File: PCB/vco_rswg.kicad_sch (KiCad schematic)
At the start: 19 parts, among them J6 VCO, Q1 2N5457, U1 LM324, U2 LM324

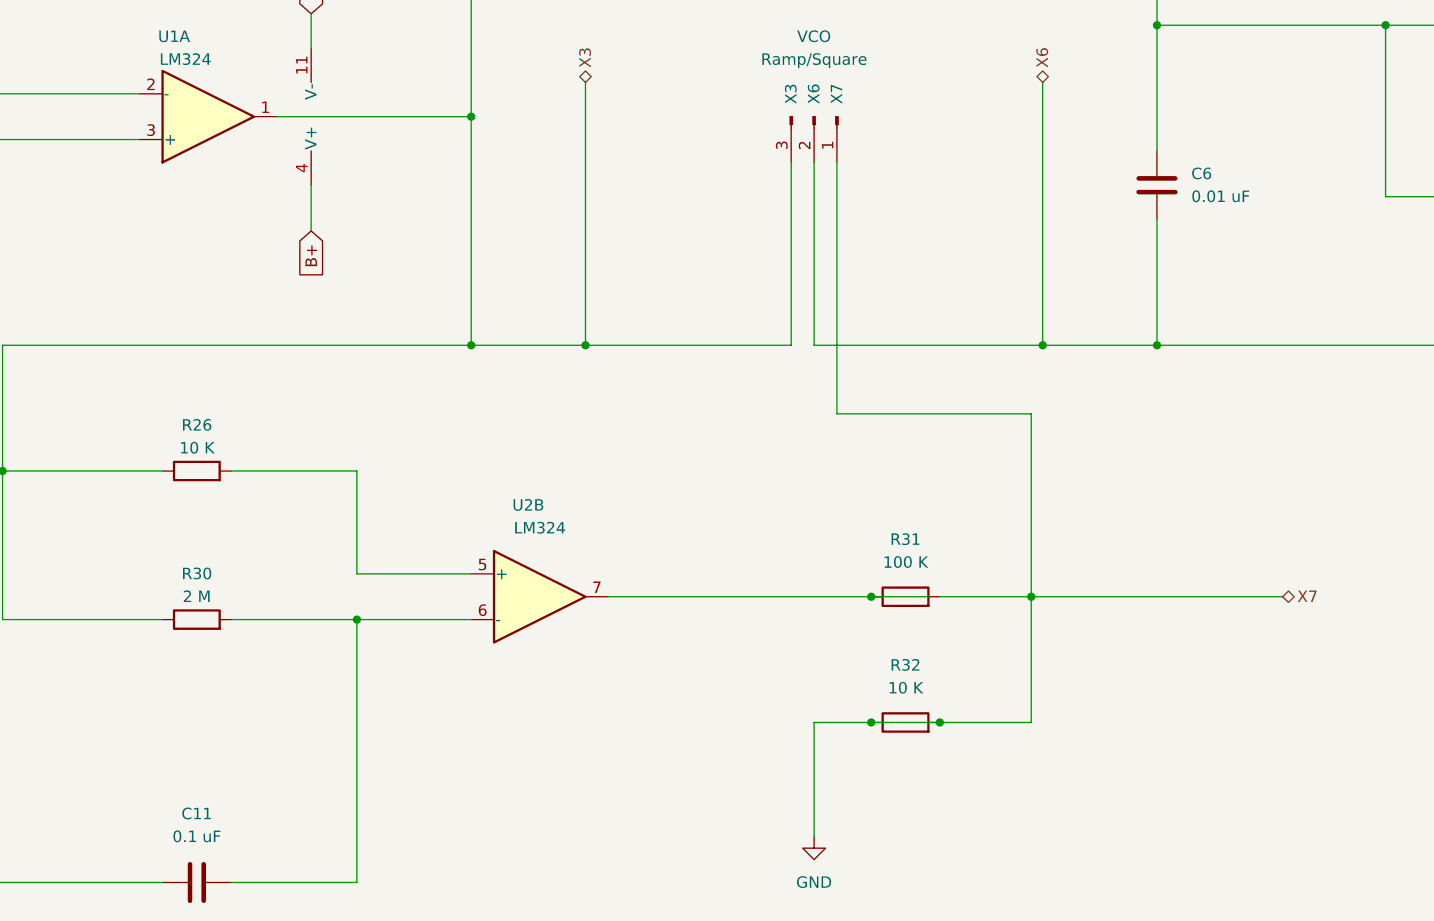
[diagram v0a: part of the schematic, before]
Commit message: Change TO-92 transistors to wide package to avoid shorting during soldering
Added B- hole for speaker
Added more vias to shorten traces
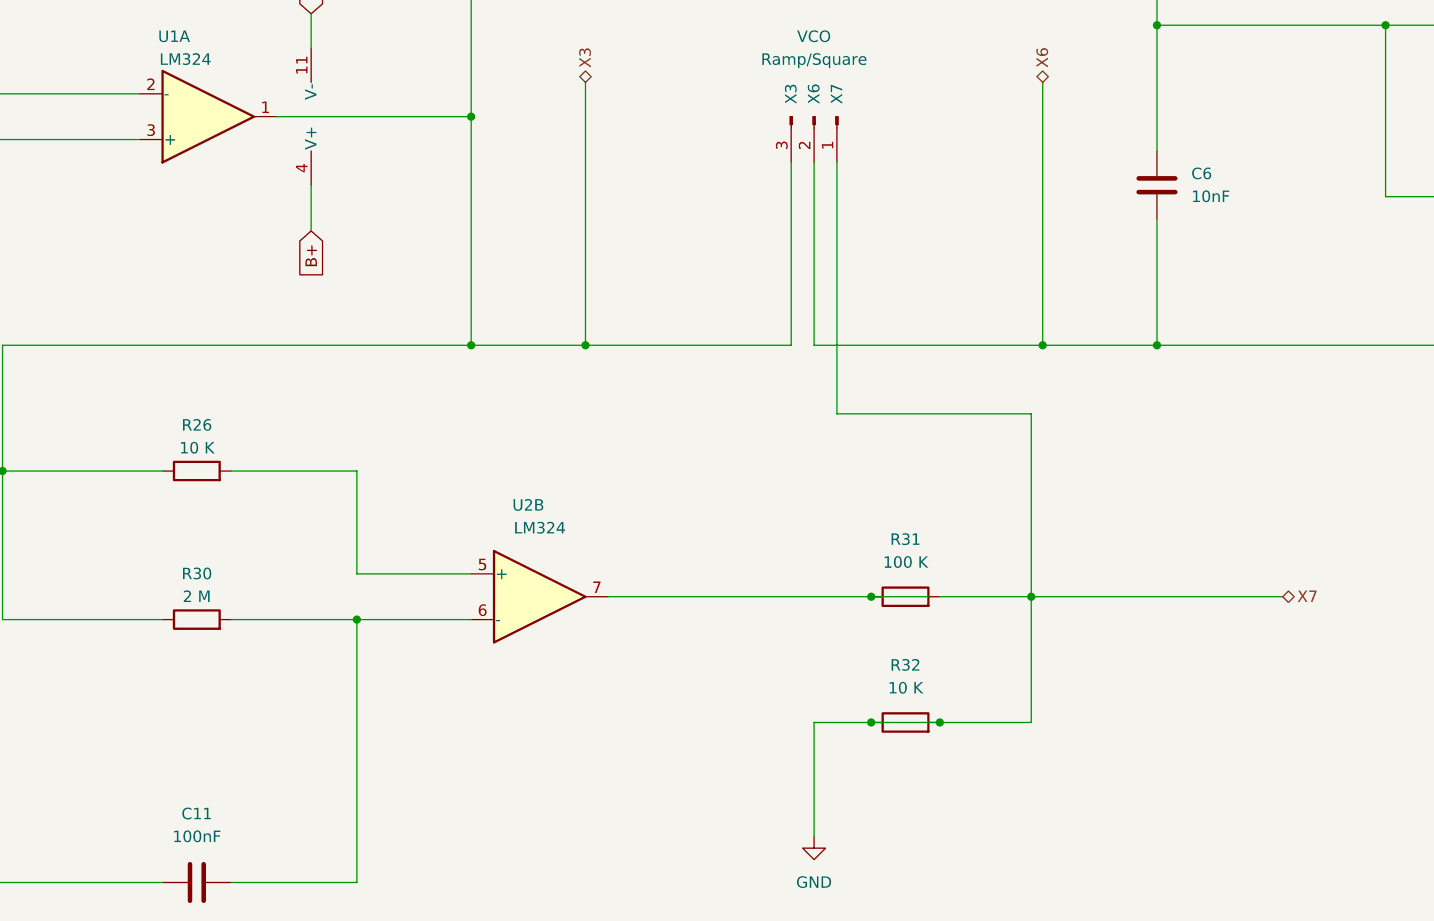
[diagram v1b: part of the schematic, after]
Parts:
- C11: value 0.1 uF -> 100nF
- C6: value 0.01 uF -> 10nF
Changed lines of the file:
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@@
 			)
 		)
-		(property "Value" "0.1 uF"
+		(property "Value" "100nF"
 			(at 58.42 172.72 90)
 			(show_name no)
@@
 		(fields_autoplaced yes)
 		(property "Reference" "C6"
-			(at 168.91 99.06 0)
+			(at 168.91 99.0599 0)
 			(show_name no)
 			(do_not_autoplace no)
@@
 			)
 		)
-		(property "Value" "0.01 uF"
-			(at 168.91 101.6 0)
+		(property "Value" "10nF"
+			(at 168.91 101.5999 0)
 			(show_name no)
 			(do_not_autoplace no)

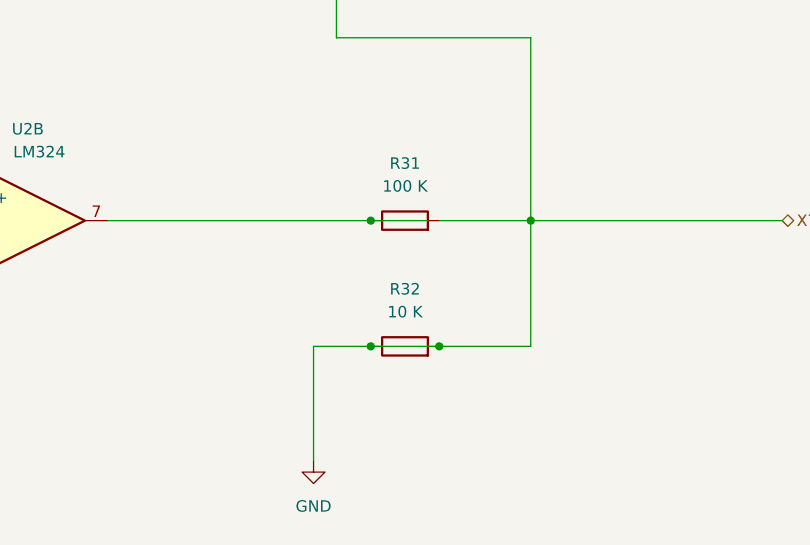
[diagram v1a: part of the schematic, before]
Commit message: Fix accidental short
Id reckon Tom tried to select these 3 traces and drag them, but the resistors didnt move along so he accidentally shorted R31, R32 and the square wave output of the VCO to the LPF
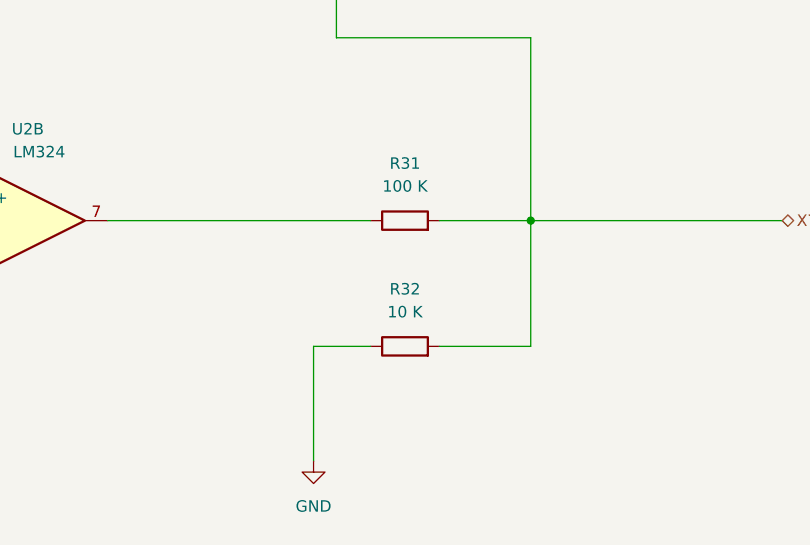
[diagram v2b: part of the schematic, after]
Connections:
- net GND: no longer J6.1 (Pin_1), R31.2, R32.2
- new net X7: J6.1 (Pin_1), R31.2, R32.2
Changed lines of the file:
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@@
-	)
-	(junction
-		(at 140.97 160.02)
-		(diameter 0)
-		(color 0 0 0 0)
 	)
 	(junction
@@
 	)
 	(junction
-		(at 133.35 146.05)
-		(diameter 0)
-		(color 0 0 0 0)
-	)
-	(junction
 		(at 88.9 118.11)
 		(diameter 0)
@@
 	)
 	(junction
-		(at 133.35 160.02)
-		(diameter 0)
-		(color 0 0 0 0)
-	)
-	(junction
 		(at 36.83 132.08)
 		(diameter 0)
@@
 	(wire
 		(pts
-			(xy 139.7 146.05) (xy 133.35 146.05)
-		)
-		(stroke
-			(width 0)
-			(type default)
-		)
-	)
-	(wire
-		(pts
 			(xy 212.09 101.6) (xy 190.5 101.6)
 		)
@@
 		)
 		(stroke
-			(width 0)
-			(type default)
-		)
-	)
-	(wire
-		(pts
-			(xy 133.35 160.02) (xy 140.97 160.02)
-		)
-		(stroke

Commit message: Necessary Changes to Schematic and PCB
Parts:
- J6: footprint Connector_PinHeader_2.00mm:PinHeader_1x03_P2.00mm_Vertical -> Connector_PinSocket_2.54mm:PinSocket_1x03_P2.54mm_Vertical
- Q1: footprint Package_TO_SOT_THT:TO-92_Inline -> Package_TO_SOT_THT:TO-92_Inline_Wide; symbol Simulation_SPICE:NJFET -> Device:Q_NJFET_DSG
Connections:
- net X3: now also Q1.2 (S); no longer Q1.3 (S)
- net at R5.1, R6.1: now also Q1.3 (G); no longer Q1.2 (G)
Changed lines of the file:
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@@
 			)
 		)
-		(property "Footprint" "Connector_PinHeader_2.00mm:PinHeader_1x03_P2.00mm_Vertical"
+		(property "Footprint" "Connector_PinSocket_2.54mm:PinSocket_1x03_P2.54mm_Vertical"
 			(at 127 92.71 0)
 			(hide yes)
@@
 	)
 	(symbol
-		(lib_id "Simulation_SPICE:NJFET")
+		(lib_id "Device:Q_NJFET_DSG")
 		(at 60.96 38.1 90)
 		(mirror x)
@@
 			)
 		)
-		(property "Footprint" "Package_TO_SOT_THT:TO-92_Inline"
+		(property "Footprint" "Package_TO_SOT_THT:TO-92_Inline_Wide"
 			(at 58.42 43.18 0)
 			(hide yes)
@@
 			)
 		)
-		(property "Description" ""
+		(property "Description" "N-JFET transistor, drain/source/gate"
 			(at 60.96 38.1 0)
 			(hide yes)
@@
 			)
 		)
-		(property "Sim.Pins" "1=D 2=G 3=S"
+		(property "Sim.Pins" "1=D 2=S 3=G"
 			(at 60.96 38.1 0)
 			(hide yes)

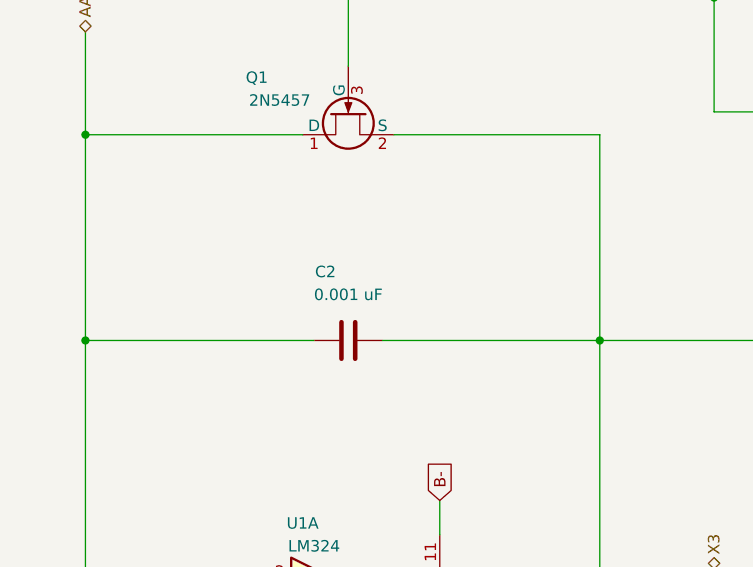
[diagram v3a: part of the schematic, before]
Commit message: Fixed grave mistake (Q10 position swapped)
Tom forgot to mirror Q10, swapping the emitter and collectors of Q10
Changed all the footprints of electrolytic caps to 5mm (i didnt find a single cap in my parts bin rated for 25V that was 4mm diameter)
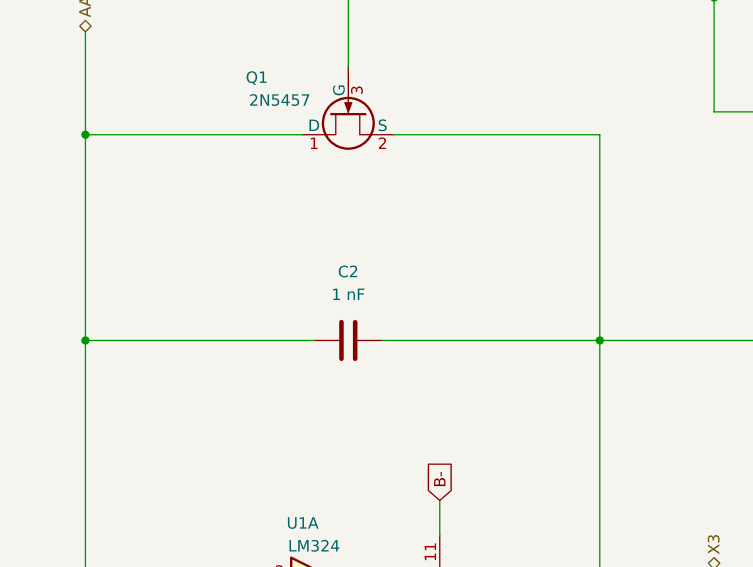
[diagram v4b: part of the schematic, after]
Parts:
- C2: value 0.001 uF -> 1 nF
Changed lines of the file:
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@@
 		(dnp no)
 		(property "Reference" "C2"
-			(at 58.42 55.88 90)
+			(at 60.96 55.88 90)
 			(show_name no)
 			(do_not_autoplace no)
@@
 			)
 		)
-		(property "Value" "0.001 uF"
+		(property "Value" "1 nF"
 			(at 60.96 58.42 90)
 			(show_name no)

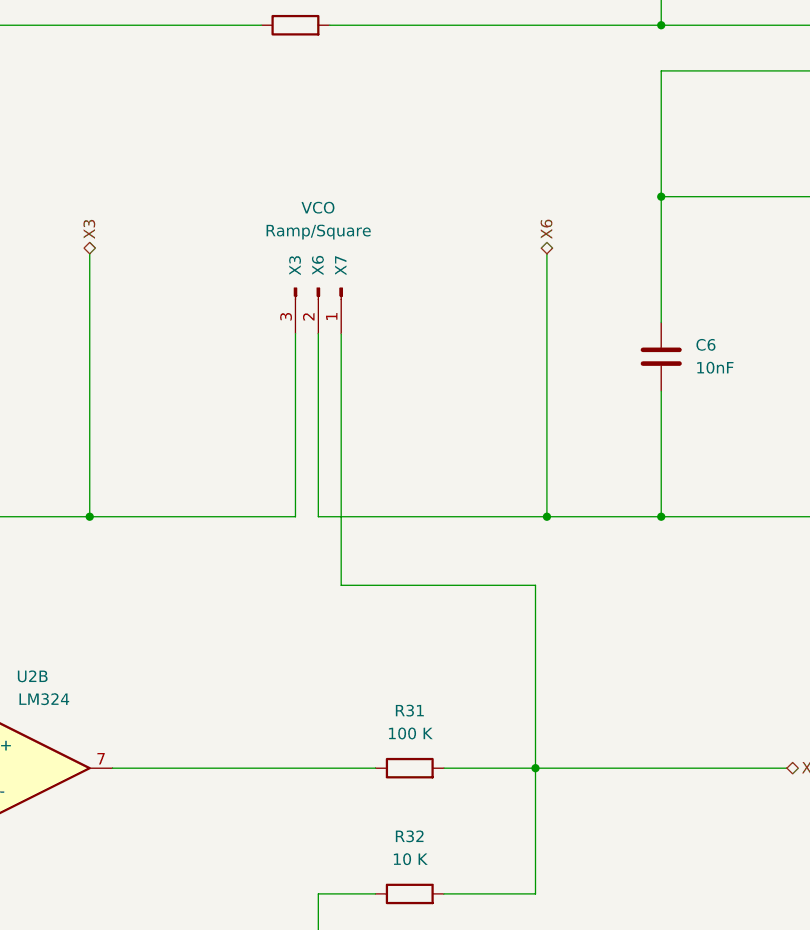
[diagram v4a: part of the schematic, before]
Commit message: Final Update
Move power pins closer to filter caps
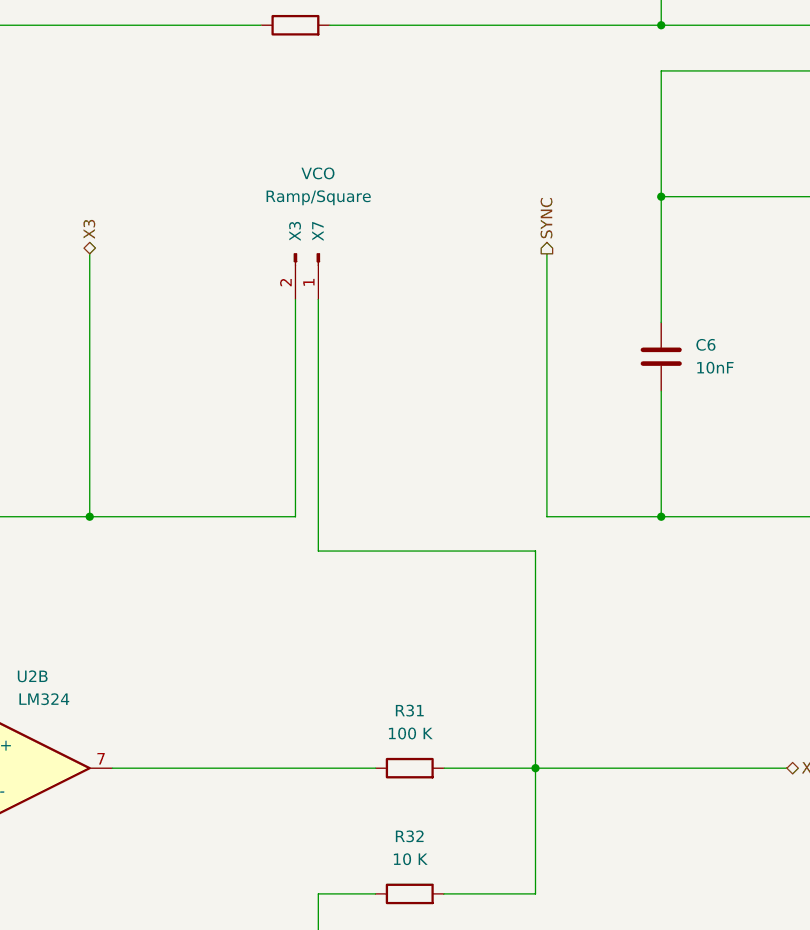
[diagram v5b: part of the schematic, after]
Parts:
- removed J6: VCO, Connector_PinSocket_2.54mm:PinSocket_1x03_P2.54mm_Vertical, symbol Connector:Conn_01x03_Pin
- added J6: VCO, Connector_PinSocket_2.54mm:PinSocket_1x02_P2.54mm_Vertical, symbol Connector:Conn_01x02_Pin
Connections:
- net X3: now also J6.2 (Pin_2)
- net X7: now also J6.1 (Pin_1)
- net X6 renamed SYNC
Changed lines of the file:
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@@
 		(color 0 0 0 0)
 	)
-	(junction
-		(at 152.4 118.11)
-		(diameter 0)
-		(color 0 0 0 0)
-	)
 	(wire
 		(pts
@@
 	(wire
 		(pts
-			(xy 151.13 125.73) (xy 151.13 146.05)
+			(xy 151.13 121.92) (xy 151.13 146.05)
 		)
 		(stroke
@@
 	(wire
 		(pts
-			(xy 129.54 125.73) (xy 151.13 125.73)
+			(xy 127 121.92) (xy 151.13 121.92)
 		)
 		(stroke
@@
 	(wire
 		(pts
-			(xy 127 97.79) (xy 127 118.11)
-		)
-		(stroke
-			(width 0)
-			(type default)
-		)
-	)
-	(wire
-		(pts
 			(xy 76.2 143.51) (xy 88.9 143.51)
 		)
@@
 	(wire
 		(pts
-			(xy 129.54 97.79) (xy 129.54 125.73)
+			(xy 127 93.98) (xy 127 121.92)
 		)
 		(stroke
@@
 	(wire
 		(pts
-			(xy 124.46 97.79) (xy 124.46 118.11)
+			(xy 124.46 93.98) (xy 124.46 118.11)
 		)
 		(stroke
@@
 		(pts
 			(xy 31.75 90.17) (xy 52.07 90.17)
-		)
-		(stroke
-			(width 0)
-			(type default)
-		)
-	)
-	(wire
-		(pts
-			(xy 127 118.11) (xy 152.4 118.11)
 		)
 		(stroke
@@
 		)
 	)
-	(hierarchical_label "X6"
-		(shape bidirectional)
+	(hierarchical_label "SYNC"
+		(shape output)
 		(at 152.4 88.9 90)
 		(effects
@@
 			)
 			(justify left)
-		)
-		(property "Bezeichnung" ""
-			(at 154.94 87.63 90)
-			(hide yes)
-			(show_name no)
-			(do_not_autoplace no)
-			(effects
-				(font
-					(size 1.27 1.27)
-					(italic yes)
-				)
-				(justify left)
-			)
 		)
 	)
@@
 					(reference "U1")
 					(unit 2)
+				)
+			)
+		)
+	)
+	(symbol
+		(lib_id "Connector:Conn_01x02_Pin")
+		(at 127 88.9 270)
+		(unit 1)
+		(body_style 1)
+		(exclude_from_sim no)
+		(in_bom yes)
+		(on_board yes)
+		(in_pos_files yes)
+		(dnp no)
+		(property "Reference" "J6"
+			(at 127 83.82 90)
+			(hide yes)
+			(show_name no)
+			(do_not_autoplace no)
+			(effects
+				(font
+					(size 1.27 1.27)
+				)
+			)
+		)
+		(property "Value" "VCO"
+			(at 127 80.01 90)
+			(show_name no)
+			(do_not_autoplace no)
+			(effects
+				(font
+					(size 1.27 1.27)
+				)
+			)
+		)
+		(property "Footprint" "Connector_PinSocket_2.54mm:PinSocket_1x02_P2.54mm_Vertical"
+			(at 127 88.9 0)
+			(hide yes)
+			(show_name no)
+			(do_not_autoplace no)
+			(effects
+				(font
+					(size 1.27 1.27)
+				)
+			)
+		)
+		(property "Datasheet" ""
+			(at 127 88.9 0)
+			(hide yes)
+			(show_name no)
+			(do_not_autoplace no)
+			(effects
+				(font
+					(size 1.27 1.27)
+				)
+			)
+		)
+		(property "Description" "Generic connector, single row, 01x02, script generated"
+			(at 127 88.9 0)
+			(hide yes)
+			(show_name no)
+			(do_not_autoplace no)
+			(effects
+				(font
+					(size 1.27 1.27)
+				)
+			)
+		)
+		(property "Wert2" "Ramp/Square"
+			(at 127 82.55 90)
+			(show_name no)
+			(do_not_autoplace no)
+			(effects
+				(font
+					(size 1.27 1.27)
+				)
+			)
+		)
+		(property "X3" "X3"
+			(at 124.46 86.36 0)
+			(show_name no)
+			(do_not_autoplace no)
+			(effects
+				(font
+					(size 1.27 1.27)
+				)
+			)
+		)
+		(property "X6" "X6"
+			(at 127 86.36 0)
+			(hide yes)
+			(show_name no)
+			(do_not_autoplace no)
+			(effects
+				(font
+					(size 1.27 1.27)
+				)
+			)
+		)
+		(property "X7" "X7"
+			(at 127 86.36 0)
+			(show_name no)
+			(do_not_autoplace no)
+			(effects
+				(font
+					(size 1.27 1.27)
+				)
+			)
+		)
+		(pin "1"
+		)
+		(pin "2"
+		)
+		(instances
+			(project "Noise Toaster PCB"
+				(path "/7be3f398-d902-4566-9ee4-0bff072cd47e/a3e9deee-1b9d-4545-a3c9-71b211642b5b"
+					(reference "J6")
+					(unit 1)
 				)
 			)
@@
 					(unit 1)
 				)
-			)
-		)
-	)
-	(symbol
-		(lib_id "Connector:Conn_01x03_Pin")
-		(at 127 92.71 270)
-		(unit 1)
-		(body_style 1)
-		(exclude_from_sim no)
-		(in_bom yes)
-		(on_board yes)
-		(in_pos_files yes)
-		(dnp no)
-		(property "Reference" "J6"
-			(at 127 87.63 90)
-			(hide yes)
-			(show_name no)
-			(do_not_autoplace no)
-			(effects
-				(font
-					(size 1.27 1.27)
-				)
-			)
-		)
-		(property "Value" "VCO"
-			(at 127 83.82 90)
-			(show_name no)
-			(do_not_autoplace no)
-			(effects
-				(font
-					(size 1.27 1.27)
-				)
-			)
-		)
-		(property "Footprint" "Connector_PinSocket_2.54mm:PinSocket_1x03_P2.54mm_Vertical"
-			(at 127 92.71 0)
-			(hide yes)
-			(show_name no)
-			(do_not_autoplace no)
-			(effects
-				(font
-					(size 1.27 1.27)
-				)
-			)
-		)
-		(property "Datasheet" ""
-			(at 127 92.71 0)
-			(hide yes)
-			(show_name no)
-			(do_not_autoplace no)
-			(effects
-				(font
-					(size 1.27 1.27)
-				)
-			)
-		)
-		(property "Description" ""
-			(at 127 92.71 0)
-			(hide yes)
-			(show_name no)
-			(do_not_autoplace no)
-			(effects
-				(font
-					(size 1.27 1.27)
-				)
-			)
-		)
-		(property "Wert2" "Ramp/Square"
-			(at 127 86.36 90)
-			(show_name no)
-			(do_not_autoplace no)
-			(effects
-				(font
-					(size 1.27 1.27)
-				)
-			)
-		)
-		(property "X3" "X3"
-			(at 124.46 90.17 0)
-			(show_name no)
-			(do_not_autoplace no)
-			(effects
-				(font
-					(size 1.27 1.27)
-				)
-			)
-		)
-		(property "X6" "X6"
-			(at 127 90.17 0)
-			(show_name no)
-			(do_not_autoplace no)
-			(effects
-				(font
-					(size 1.27 1.27)
-				)
-			)
-		)
-		(property "X7" "X7"
-			(at 129.54 90.17 0)
-			(show_name no)
-			(do_not_autoplace no)
-			(effects
-				(font
-					(size 1.27 1.27)
-				)
-			)
-		)
-		(pin "1"
-		)
-		(pin "2"
-		)
-		(pin "3"
-		)
-		(instances
-			(project "Noise Toaster PCB"
-				(path "/7be3f398-d902-4566-9ee4-0bff072cd47e/a3e9deee-1b9d-4545-a3c9-71b211642b5b"
-					(reference "J6")
-					(unit 1)
-				)
